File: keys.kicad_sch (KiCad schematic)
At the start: 167 parts, among them SW1 RotaryEncoder_Switch, U11 SLSS49E-3, U12 SLSS49E-3, U13 SLSS49E-3, U14 SLSS49E-3, U15 SLSS49E-3, U16 SLSS49E-3, U17 SLSS49E-3, U18 SLSS49E-3, U19 SLSS49E-3, U2 SLSS49E-3, U20 SLSS49E-3, U21 SLSS49E-3, U22 SLSS49E-3, U23 SLSS49E-3, U24 SLSS49E-3, U25 SLSS49E-3, U26 SLSS49E-3, U27 SLSS49E-3, U28 SLSS49E-3, U29 SLSS49E-3, U30 SLSS49E-3, U31 SLSS49E-3, U32 SLSS49E-3, U33 SLSS49E-3, U34 SLSS49E-3, U35 SLSS49E-3, U36 SLSS49E-3, U37 SLSS49E-3, U38 SLSS49E-3, U39 SLSS49E-3, U4 SLSS49E-3, U40 SLSS49E-3, U41 SLSS49E-3, U42 SLSS49E-3, U43 SLSS49E-3, U44 SLSS49E-3, U45 SLSS49E-3, U46 SLSS49E-3, U47 SLSS49E-3, U48 SLSS49E-3, U49 SLSS49E-3, U50 SLSS49E-3, U51 SLSS49E-3, U52 SLSS49E-3, U53 SLSS49E-3, U54 SLSS49E-3, U55 SLSS49E-3, U56 SLSS49E-3, U57 SLSS49E-3, U58 SLSS49E-3, U59 SLSS49E-3, U60 SLSS49E-3, U61 SLSS49E-3, U62 SLSS49E-3, U63 SLSS49E-3, U64 SLSS49E-3, U65 SLSS49E-3, U66 SLSS49E-3, U67 SLSS49E-3, U68 SLSS49E-3, U69 SLSS49E-3, U70 SLSS49E-3, U71 SLSS49E-3, U72 SLSS49E-3, U73 SLSS49E-3, U74 SLSS49E-3, U75 SLSS49E-3, U76 SLSS49E-3, U77 SLSS49E-3, U78 SLSS49E-3, U79 SLSS49E-3, U80 SLSS49E-3, U81 SLSS49E-3, U82 SLSS49E-3, U83 SLSS49E-3, U84 SLSS49E-3, U85 SLSS49E-3, U86 SLSS49E-3, U87 SLSS49E-3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

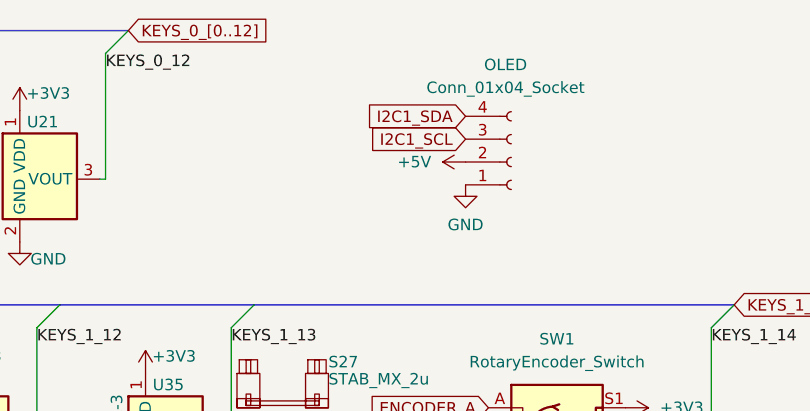
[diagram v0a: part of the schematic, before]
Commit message: change some pins
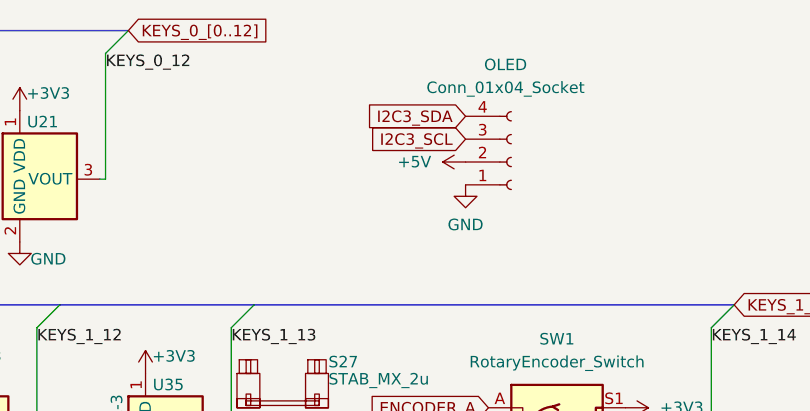
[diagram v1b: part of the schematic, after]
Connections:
- net I2C1_SCL renamed I2C3_SCL
- net I2C1_SDA renamed I2C3_SDA
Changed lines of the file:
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@@
     )
   )
-  (global_label "I2C1_SDA" (shape input) (at 359.41 28.575 180) (fields_autoplaced)
+  (global_label "I2C3_SDA" (shape input) (at 359.41 28.575 180) (fields_autoplaced)
     (effects (font (size 1.27 1.27)) (justify right))
     (property "Intersheetrefs" "${INTERSHEET_REFS}" (at 347.5953 28.575 0)
@@
     )
   )
-  (global_label "I2C1_SCL" (shape input) (at 359.41 31.115 180) (fields_autoplaced)
+  (global_label "I2C3_SCL" (shape input) (at 359.41 31.115 180) (fields_autoplaced)
     (effects (font (size 1.27 1.27)) (justify right))
     (property "Intersheetrefs" "${INTERSHEET_REFS}" (at 347.6558 31.115 0)

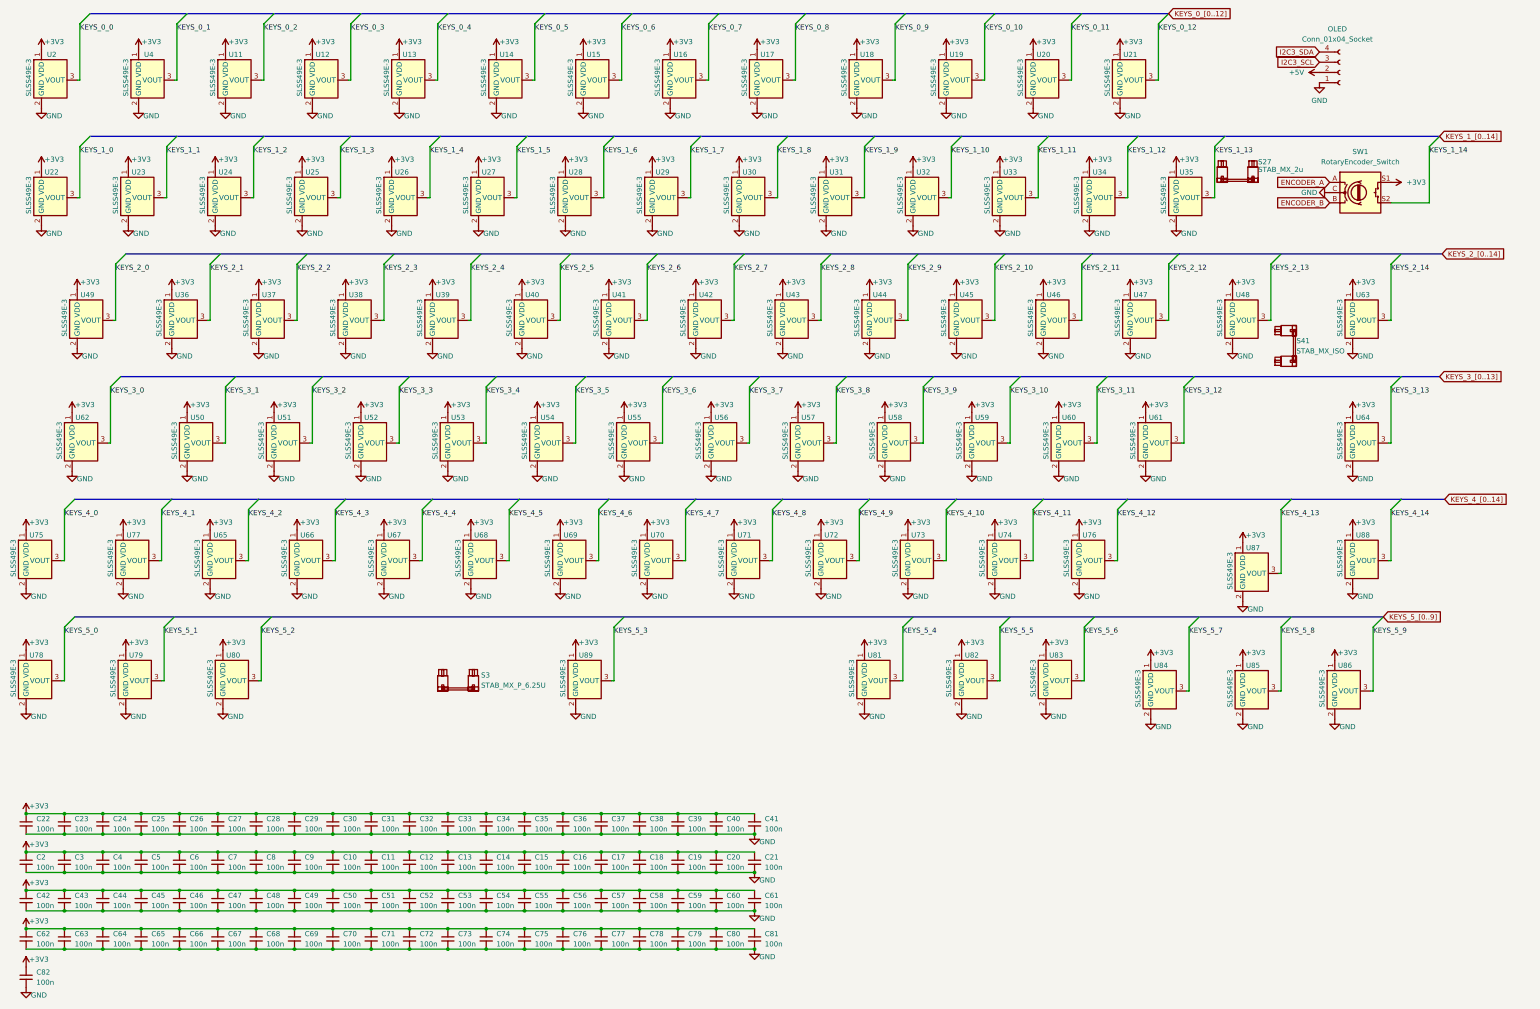
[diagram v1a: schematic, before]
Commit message: restructure schematic to use hierarchical sheets
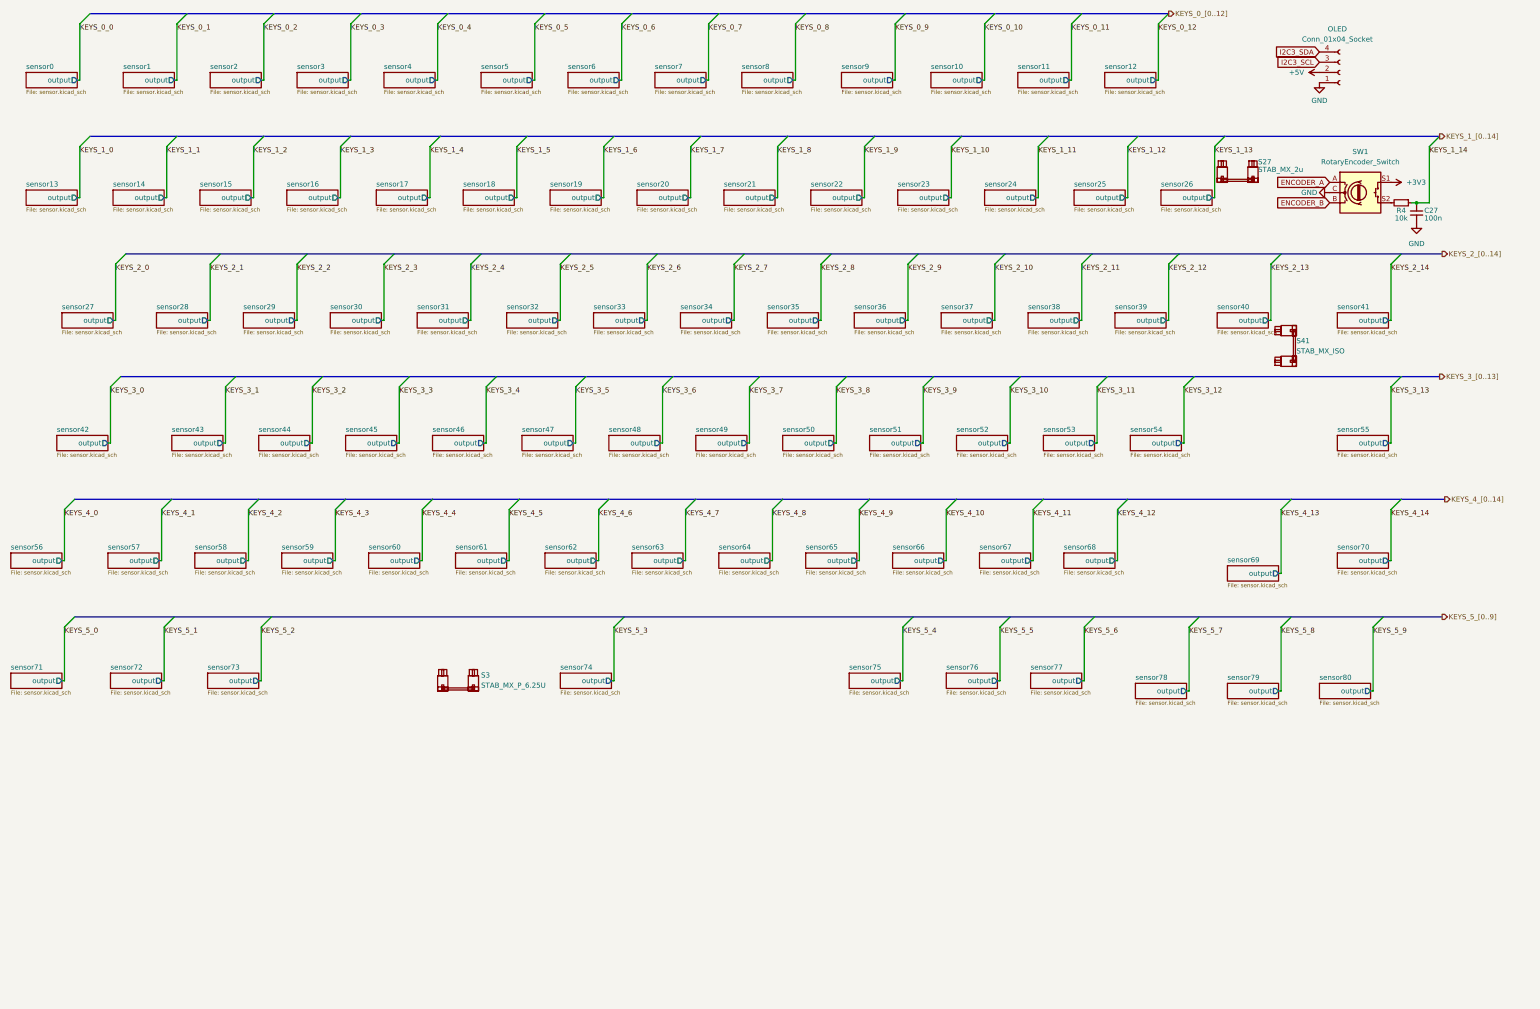
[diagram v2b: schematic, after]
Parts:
- removed C10, C11, C12, C13, C14, C15, C16, C17, C18, C19, C2, C20, C21, C22, C23, C24, C25, C26, C28, C29, C3, C30, C31, C32, C33, C34, C35, C36, C37, C38, C39, C4, C40, C41, C42, C43, C44, C45, C46, C47, C48, C49, C5, C50, C51, C52, C53, C54, C55, C56, C57, C58, C59, C6, C60, C61, C62, C63, C64, C65, C66, C67, C68, C69, C7, C70, C71, C72, C73, C74, C75, C76, C77, C78, C79, C8, C80, C81, C82, C9: 100n, Capacitor_SMD:C_0402_1005Metric, symbol Device:C_Small
- removed U11, U12, U13, U14, U15, U16, U17, U18, U19, U2, U20, U21, U22, U23, U24, U25, U26, U27, U28, U29, U30, U31, U32, U33, U34, U35, U36, U37, U38, U39, U4, U40, U41, U42, U43, U44, U45, U46, U47, U48, U50, U51, U52, U53, U54, U55, U56, U57, U58, U59, U60, U61, U63, U64, U65, U66, U67, U68, U69, U70, U71, U72, U73, U74, U77, U81, U82, U83, U84, U85, U86, U87, U88, U89: SLSS49E-3, MoonBoard:SLSS49E-3 with MX holes, symbol MoonBoard:SLSS49E-3_with_switch
- removed U49: SLSS49E-3, MoonBoard:SLSS49E-3 with 1.5u MX holes, symbol MoonBoard:SLSS49E-3_with_switch
- removed U62, U76: SLSS49E-3, MoonBoard:SLSS49E-3 with 1.75u MX holes, symbol MoonBoard:SLSS49E-3_with_switch
- removed U75, U78, U79, U80: SLSS49E-3, MoonBoard:SLSS49E-3 with 1.25u MX holes, symbol MoonBoard:SLSS49E-3_with_switch
- added R4: 10k, Resistor_SMD:R_0402_1005Metric, symbol Device:R_Small
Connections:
- net +3V3: no longer C27.1
- net KEYS_1_14: now also C27.1, R4.1; no longer SW1.S2
- new net: R4.2, SW1.S2
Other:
- added sheet sensor0 (sensor.kicad_sch)
- added sheet sensor1 (sensor.kicad_sch)
- added sheet sensor10 (sensor.kicad_sch)
- added sheet sensor11 (sensor.kicad_sch)
- added sheet sensor12 (sensor.kicad_sch)
- added sheet sensor13 (sensor.kicad_sch)
- added sheet sensor14 (sensor.kicad_sch)
- added sheet sensor15 (sensor.kicad_sch)
- added sheet sensor16 (sensor.kicad_sch)
- added sheet sensor17 (sensor.kicad_sch)
- added sheet sensor18 (sensor.kicad_sch)
- added sheet sensor19 (sensor.kicad_sch)
- added sheet sensor2 (sensor.kicad_sch)
- added sheet sensor20 (sensor.kicad_sch)
- added sheet sensor21 (sensor.kicad_sch)
- added sheet sensor22 (sensor.kicad_sch)
- added sheet sensor23 (sensor.kicad_sch)
- added sheet sensor24 (sensor.kicad_sch)
- added sheet sensor25 (sensor.kicad_sch)
- added sheet sensor26 (sensor.kicad_sch)
- added sheet sensor27 (sensor.kicad_sch)
- added sheet sensor28 (sensor.kicad_sch)
- added sheet sensor29 (sensor.kicad_sch)
- added sheet sensor3 (sensor.kicad_sch)
- added sheet sensor30 (sensor.kicad_sch)
- added sheet sensor31 (sensor.kicad_sch)
- added sheet sensor32 (sensor.kicad_sch)
- added sheet sensor33 (sensor.kicad_sch)
- added sheet sensor34 (sensor.kicad_sch)
- added sheet sensor35 (sensor.kicad_sch)
- added sheet sensor36 (sensor.kicad_sch)
- added sheet sensor37 (sensor.kicad_sch)
- added sheet sensor38 (sensor.kicad_sch)
- added sheet sensor39 (sensor.kicad_sch)
- added sheet sensor4 (sensor.kicad_sch)
- added sheet sensor40 (sensor.kicad_sch)
- added sheet sensor41 (sensor.kicad_sch)
- added sheet sensor42 (sensor.kicad_sch)
- added sheet sensor43 (sensor.kicad_sch)
- added sheet sensor44 (sensor.kicad_sch)
- added sheet sensor45 (sensor.kicad_sch)
- added sheet sensor46 (sensor.kicad_sch)
- added sheet sensor47 (sensor.kicad_sch)
- added sheet sensor48 (sensor.kicad_sch)
- added sheet sensor49 (sensor.kicad_sch)
- added sheet sensor5 (sensor.kicad_sch)
- added sheet sensor50 (sensor.kicad_sch)
- added sheet sensor51 (sensor.kicad_sch)
- added sheet sensor52 (sensor.kicad_sch)
- added sheet sensor53 (sensor.kicad_sch)
- added sheet sensor54 (sensor.kicad_sch)
- added sheet sensor55 (sensor.kicad_sch)
- added sheet sensor56 (sensor.kicad_sch)
- added sheet sensor57 (sensor.kicad_sch)
- added sheet sensor58 (sensor.kicad_sch)
- added sheet sensor59 (sensor.kicad_sch)
- added sheet sensor6 (sensor.kicad_sch)
- added sheet sensor60 (sensor.kicad_sch)
- added sheet sensor61 (sensor.kicad_sch)
- added sheet sensor62 (sensor.kicad_sch)
- added sheet sensor63 (sensor.kicad_sch)
- added sheet sensor64 (sensor.kicad_sch)
- added sheet sensor65 (sensor.kicad_sch)
- added sheet sensor66 (sensor.kicad_sch)
- added sheet sensor67 (sensor.kicad_sch)
- added sheet sensor68 (sensor.kicad_sch)
- added sheet sensor69 (sensor.kicad_sch)
- added sheet sensor7 (sensor.kicad_sch)
- added sheet sensor70 (sensor.kicad_sch)
- added sheet sensor71 (sensor.kicad_sch)
- added sheet sensor72 (sensor.kicad_sch)
- added sheet sensor73 (sensor.kicad_sch)
- added sheet sensor74 (sensor.kicad_sch)
- added sheet sensor75 (sensor.kicad_sch)
- added sheet sensor76 (sensor.kicad_sch)
- added sheet sensor77 (sensor.kicad_sch)
- added sheet sensor78 (sensor.kicad_sch)
- added sheet sensor79 (sensor.kicad_sch)
- added sheet sensor8 (sensor.kicad_sch)
- added sheet sensor80 (sensor.kicad_sch)
- added sheet sensor9 (sensor.kicad_sch)

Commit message: fix sheet numbering
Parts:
- renumbered S27 to S1, S41 to S2

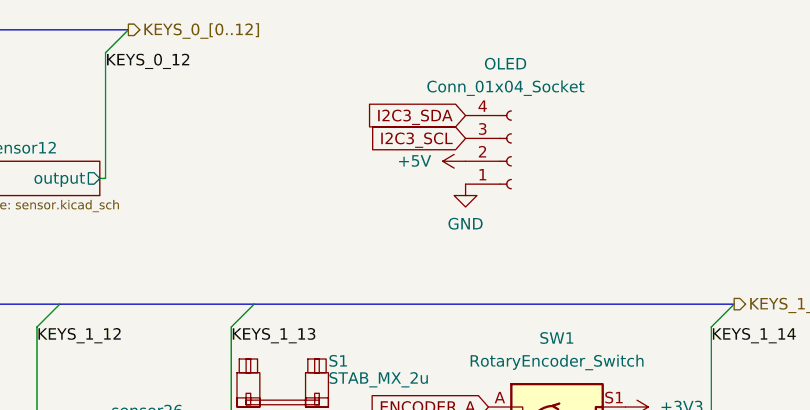
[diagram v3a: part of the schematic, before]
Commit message: finish most routing
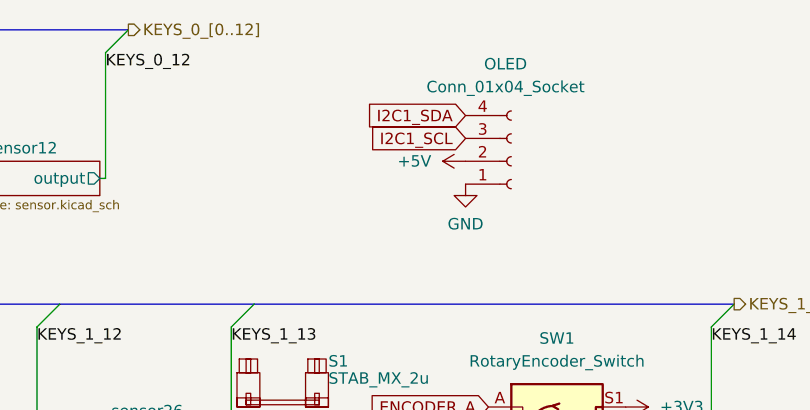
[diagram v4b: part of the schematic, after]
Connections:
- net I2C3_SCL renamed I2C1_SCL
- net I2C3_SDA renamed I2C1_SDA
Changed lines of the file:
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@@
     (effects (font (size 1.27 1.27)) (justify left bottom))
   )
-  (global_label "I2C3_SDA" (shape input) (at 359.41 28.575 180) (fields_autoplaced)
+  (global_label "I2C1_SDA" (shape input) (at 359.41 28.575 180) (fields_autoplaced)
     (effects (font (size 1.27 1.27)) (justify right))
     (property "Intersheetrefs" "${INTERSHEET_REFS}" (at 347.5953 28.575 0)
@@
     )
   )
-  (global_label "I2C3_SCL" (shape input) (at 359.41 31.115 180) (fields_autoplaced)
+  (global_label "I2C1_SCL" (shape input) (at 359.41 31.115 180) (fields_autoplaced)
     (effects (font (size 1.27 1.27)) (justify right))
     (property "Intersheetrefs" "${INTERSHEET_REFS}" (at 347.6558 31.115 0)

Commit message: finish routing
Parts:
- removed C27: 100n, Capacitor_SMD:C_0402_1005Metric, symbol Device:C_Small
- removed OLED: Conn_01x04_Socket, MoonBoard:OLED Module, symbol Connector:Conn_01x04_Socket
- removed R4: 10k, Resistor_SMD:R_0402_1005Metric, symbol Device:R_Small
- removed SW1: RotaryEncoder_Switch, PCM_marbastlib-various:ROT_Alps_EC11E-Switch, symbol Device:RotaryEncoder_Switch

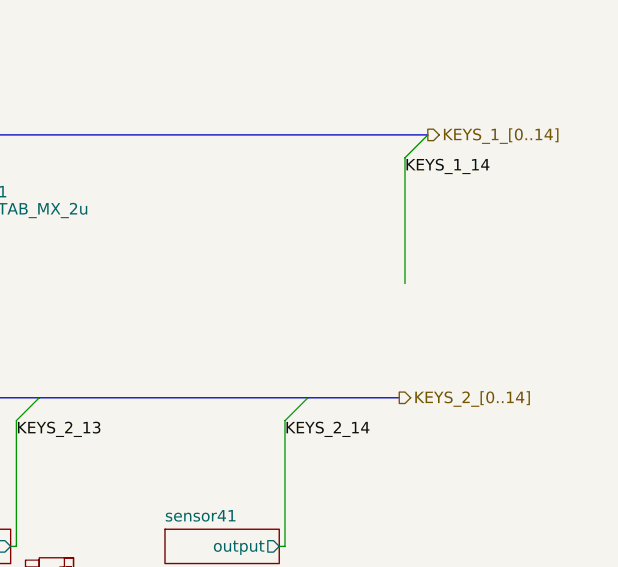
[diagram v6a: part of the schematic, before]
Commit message: add reverse polarity protection to LDO
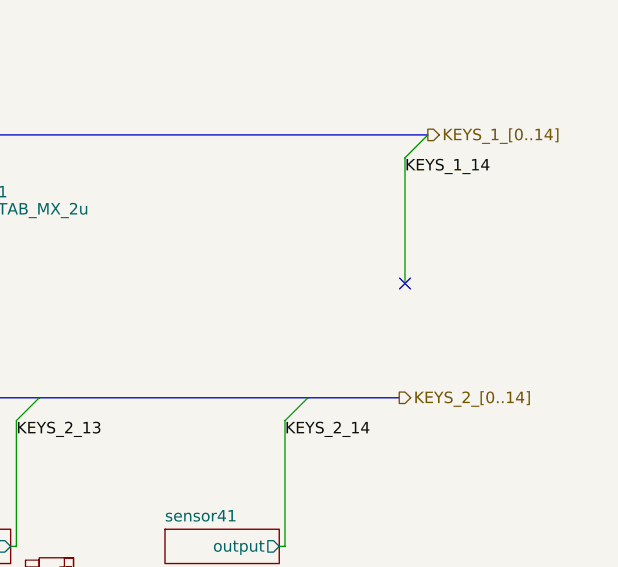
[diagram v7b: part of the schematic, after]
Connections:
- no-connect marks 0 -> 1
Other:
- title: (none) -> MoonBoard
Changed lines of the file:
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@@
 (kicad_sch (version 20230121) (generator eeschema)
   (paper "A3")
+  (title_block
+    (title "MoonBoard")
+  )
+  (no_connect (at 390.525 66.04))
   (bus_entry (at 75.565 21.59) (size 2.54 -2.54)
     (stroke (width 0) (type default))
